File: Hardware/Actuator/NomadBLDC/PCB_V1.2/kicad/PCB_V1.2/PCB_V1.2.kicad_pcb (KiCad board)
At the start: 4 copper layers, 38.9 x 37.5 mm, 66 parts, among them Q1 TPH, Q2 TPH, Q3 TPH, Q4 TPH, Q5 TPH, Q6 TPH

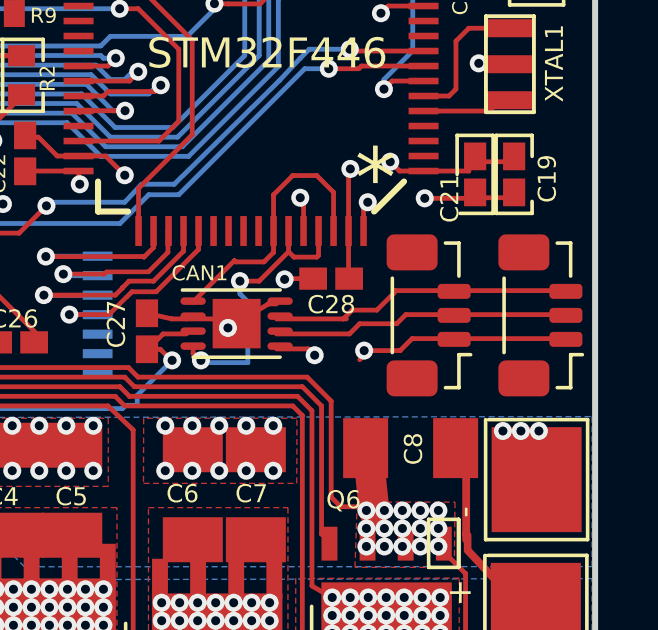
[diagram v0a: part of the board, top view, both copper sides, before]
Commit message: changes to value names of PCB
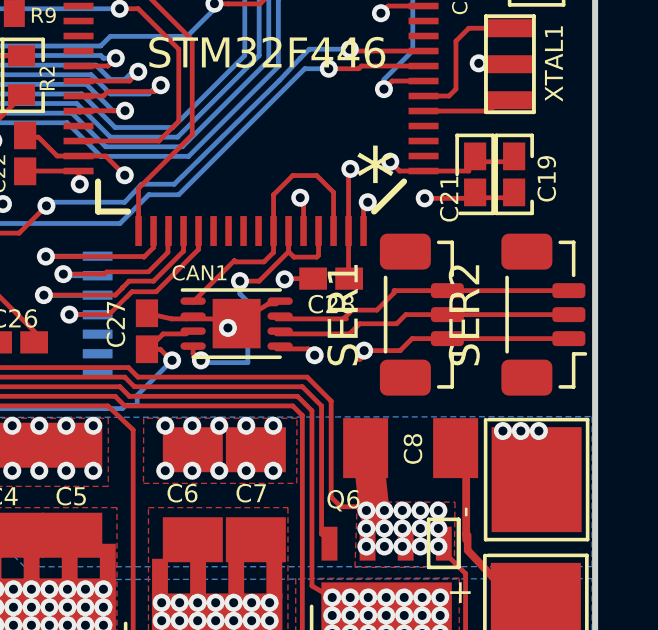
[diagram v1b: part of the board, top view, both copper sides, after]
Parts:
- C1, C2, C3, C4, C5, C6, C7, C8: value 10 -> 10uF, 50v
- C10, C13: value .1 uF -> 0.1uF, 50v
- C12: value 22 uF -> 22uF
- C14: value 47 nF -> 47nF, 50v
- C15: value 1 uF -> 1uF
- C16: value 1 uF -> 1uF, 50v
- C17: value 4.7 -> 4.7uF
- C26, C27, C28: value .1 uF -> .1uF
- C9: value 10 uF, 50v -> 10uF, 50v
- moved SER1 0.23 mm to (190.4, 118.8)
- moved SER2 0.10 mm to (194.5, 118.8)
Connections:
- YCAP1 pad 2: /N$4 -> (no net)
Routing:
- net /N$4: track 3.21 -> 0.00 mm, vias 1 -> 0
- net (no net): track 0.00 -> 3.21 mm, vias 0 -> 1
